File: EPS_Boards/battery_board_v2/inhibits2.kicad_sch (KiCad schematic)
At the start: 6 parts

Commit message: eps: battery board: added AND gate for power control and cleaned up global labels
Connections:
- net EN-D1 is gone; now on net PCM_IN: U?. (VCC)
- net PCM is gone; now on net PCM_IN: C?.2, C?.2, R?.2, U?. (VCC)
- net PCM_IN: now reaches U?. (VCC)
- net VIN renamed HIGH_INHIB_IN
- new net EN_D1: U?. (VCC)
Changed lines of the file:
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@@
     (stroke (width 0) (type default) (color 0 0 0 0))
   )
-  (polyline (pts (xy 245.11 34.29) (xy 245.11 111.76))
+  (polyline (pts (xy 248.92 34.29) (xy 248.92 111.76))
     (stroke (width 0) (type default) (color 0 0 0 0))
   )
@@
     (stroke (width 0) (type default) (color 0 0 0 0))
   )
-  (polyline (pts (xy 144.78 34.29) (xy 245.11 34.29))
+  (polyline (pts (xy 135.89 34.925) (xy 248.92 34.29))
     (stroke (width 0) (type default) (color 0 0 0 0))
   )
@@
     (stroke (width 0) (type default) (color 0 0 0 0))
   )
-  (polyline (pts (xy 245.11 111.76) (xy 144.78 111.76))
+  (polyline (pts (xy 248.92 111.76) (xy 135.89 112.395))
     (stroke (width 0) (type default) (color 0 0 0 0))
   )
@@
     (stroke (width 0) (type default) (color 0 0 0 0))
   )
-  (polyline (pts (xy 144.78 111.76) (xy 144.78 34.29))
+  (polyline (pts (xy 135.89 112.395) (xy 135.89 34.925))
     (stroke (width 0) (type default) (color 0 0 0 0))
   )
@@
     (effects (font (size 1.27 1.27)) (justify left bottom))
   )
-  (global_label "VIN" (shape input) (at 153.67 44.45 180) (fields_autoplaced)
+  (global_label "HIGH_INHIB_IN" (shape input) (at 153.67 44.45 180) (fields_autoplaced)
     (effects (font (size 1.27 1.27)) (justify right))
-    (property "Intersheet References" "${INTERSHEET_REFS}" (id 0) (at 148.322 44.3706 0)
+    (property "Intersheet References" "${INTERSHEET_REFS}" (id 0) (at 137.7991 44.3706 0)
       (effects (font (size 1.27 1.27)) (justify right) hide)
     )
@@
     )
   )
-  (global_label "EN-D1" (shape input) (at 180.34 81.28 180) (fields_autoplaced)
+  (global_label "EN_D1" (shape input) (at 180.34 81.28 180) (fields_autoplaced)
     (effects (font (size 1.27 1.27)) (justify right))
-    (property "Intersheet References" "${INTERSHEET_REFS}" (id 0) (at 171.4844 81.2006 0)
+    (property "Intersheet References" "${INTERSHEET_REFS}" (id 0) (at 172.0891 81.2006 0)
       (effects (font (size 1.27 1.27)) (justify right) hide)
     )
@@
     )
   )
-  (global_label "PCM" (shape input) (at 237.49 44.45 0) (fields_autoplaced)
+  (global_label "PCM_IN" (shape input) (at 237.49 44.45 0) (fields_autoplaced)
     (effects (font (size 1.27 1.27)) (justify left))
-    (property "Intersheet References" "${INTERSHEET_REFS}" (id 0) (at 243.8056 44.3706 0)
+    (property "Intersheet References" "${INTERSHEET_REFS}" (id 0) (at 246.7085 44.3706 0)
       (effects (font (size 1.27 1.27)) (justify left) hide)
     )

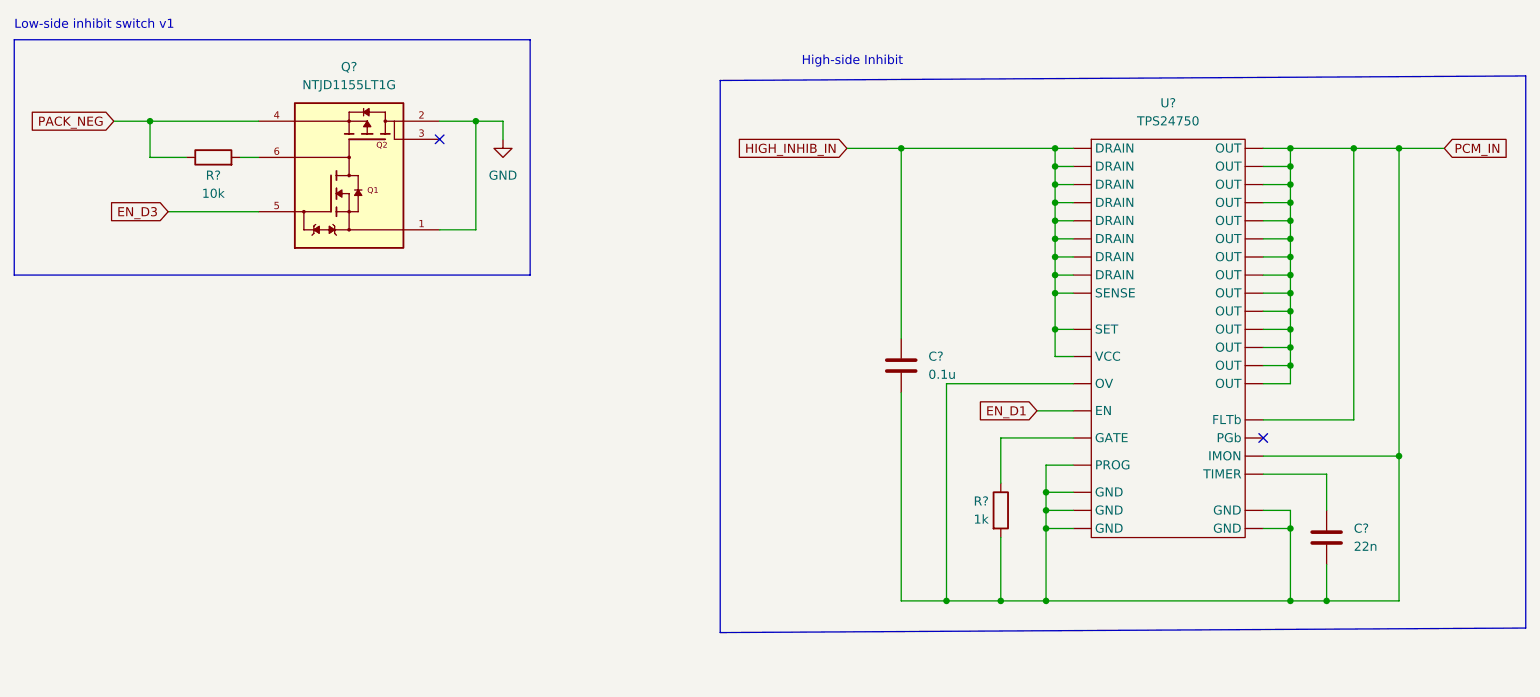
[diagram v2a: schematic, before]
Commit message: eps: battery board: finializing schematic
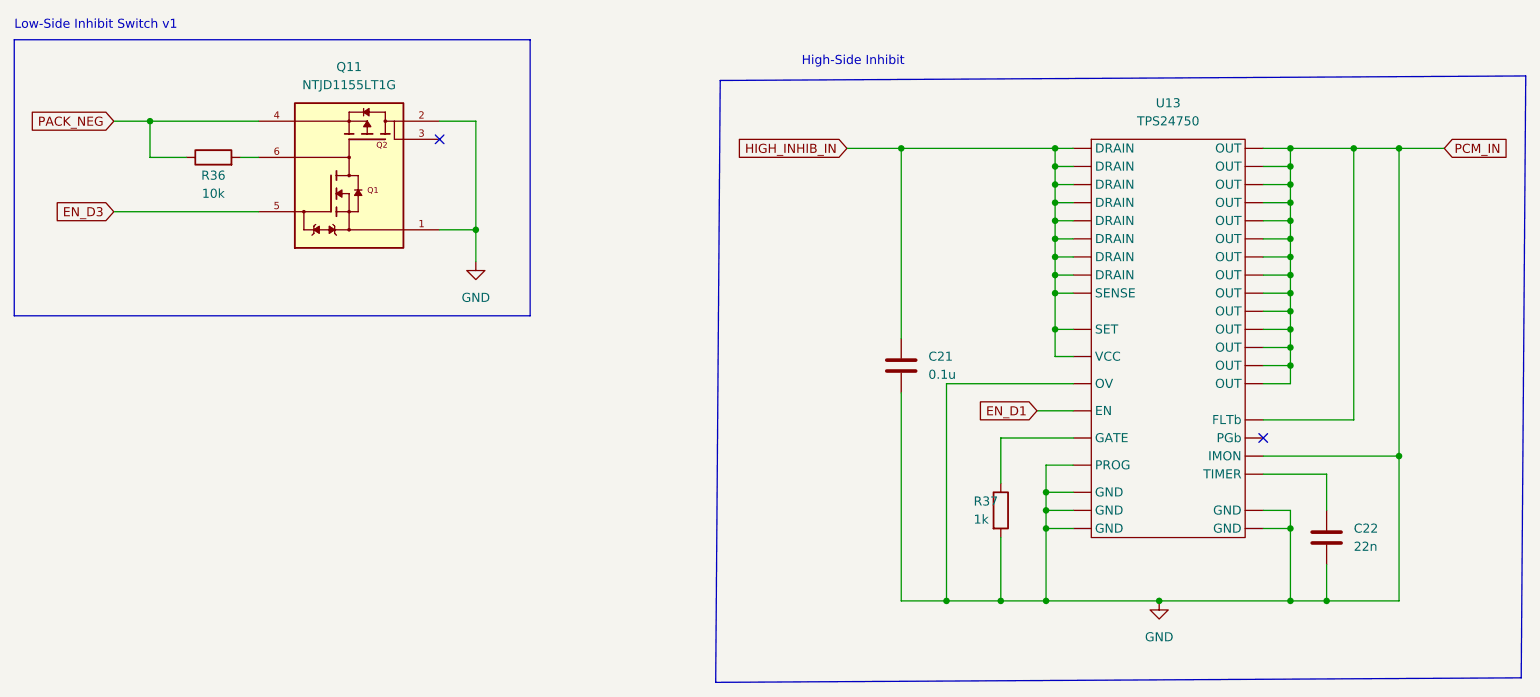
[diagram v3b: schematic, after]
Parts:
- gave numbers to parts that had none: 6
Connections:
- net GND: now also C21.2, C22.2, R37.2, U13. (VCC)
- removed net PCM_IN: C21.2, C22.2, R37.2, U13. (VCC)
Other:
- note added: "High-Side Inhibit"
- note added: "Low-Side Inhibit Switch v1"
- note removed: "High-side Inhibit"
- note removed: "Low-side inhibit switch v1"
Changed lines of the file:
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@@
   (junction (at 215.9 72.39) (diameter 0) (color 0 0 0 0)
   )
+  (junction (at 197.485 107.95) (diameter 0) (color 0 0 0 0)
+  )
   (junction (at 182.88 46.99) (diameter 0) (color 0 0 0 0)
   )
@@
   (junction (at 181.61 97.79) (diameter 0) (color 0 0 0 0)
   )
-  (junction (at 101.6 40.64) (diameter 0) (color 0 0 0 0)
+  (junction (at 101.6 55.88) (diameter 0) (color 0 0 0 0)
   )
   (junction (at 167.64 107.95) (diameter 0) (color 0 0 0 0)
@@
     (stroke (width 0) (type default) (color 0 0 0 0))
   )
+  (wire (pts (xy 197.485 107.95) (xy 215.9 107.95))
+    (stroke (width 0) (type default) (color 0 0 0 0))
+  )
   (wire (pts (xy 215.9 72.39) (xy 215.9 74.93))
     (stroke (width 0) (type default) (color 0 0 0 0))
@@
     (stroke (width 0) (type default) (color 0 0 0 0))
   )
-  (wire (pts (xy 181.61 107.95) (xy 215.9 107.95))
+  (wire (pts (xy 181.61 107.95) (xy 197.485 107.95))
     (stroke (width 0) (type default) (color 0 0 0 0))
   )
@@
     (stroke (width 0) (type default) (color 0 0 0 0))
   )
-  (polyline (pts (xy 248.92 34.29) (xy 248.92 111.76))
-    (stroke (width 0) (type default) (color 0 0 0 0))
-  )
-  (polyline (pts (xy 109.22 62.23) (xy 109.22 29.21))
+  (polyline (pts (xy 248.92 34.29) (xy 248.285 118.745))
+    (stroke (width 0) (type default) (color 0 0 0 0))
+  )
+  (polyline (pts (xy 109.22 67.945) (xy 109.22 29.21))
     (stroke (width 0) (type default) (color 0 0 0 0))
   )
@@
     (stroke (width 0) (type default) (color 0 0 0 0))
   )
-  (wire (pts (xy 58.42 53.34) (xy 71.12 53.34))
+  (wire (pts (xy 50.8 53.34) (xy 71.12 53.34))
     (stroke (width 0) (type default) (color 0 0 0 0))
   )
@@
     (stroke (width 0) (type default) (color 0 0 0 0))
   )
+  (wire (pts (xy 101.6 60.325) (xy 101.6 55.88))
+    (stroke (width 0) (type default) (color 0 0 0 0))
+  )
   (wire (pts (xy 182.88 49.53) (xy 182.88 52.07))
     (stroke (width 0) (type default) (color 0 0 0 0))
@@
     (stroke (width 0) (type default) (color 0 0 0 0))
   )
-  (wire (pts (xy 101.6 40.64) (xy 105.41 40.64))
-    (stroke (width 0) (type default) (color 0 0 0 0))
-  )
   (wire (pts (xy 175.26 99.06) (xy 175.26 107.95))
     (stroke (width 0) (type default) (color 0 0 0 0))
@@
     (stroke (width 0) (type default) (color 0 0 0 0))
   )
-  (polyline (pts (xy 248.92 111.76) (xy 135.89 112.395))
+  (polyline (pts (xy 248.285 118.745) (xy 135.255 119.38))
     (stroke (width 0) (type default) (color 0 0 0 0))
   )
@@
     (stroke (width 0) (type default) (color 0 0 0 0))
   )
-  (polyline (pts (xy 36.83 29.21) (xy 36.83 62.23))
+  (polyline (pts (xy 36.83 29.21) (xy 36.83 67.945))
     (stroke (width 0) (type default) (color 0 0 0 0))
   )
@@
     (stroke (width 0) (type default) (color 0 0 0 0))
   )
-  (polyline (pts (xy 36.83 62.23) (xy 109.22 62.23))
+  (polyline (pts (xy 36.83 67.945) (xy 109.22 67.945))
     (stroke (width 0) (type default) (color 0 0 0 0))
   )
@@
     (stroke (width 0) (type default) (color 0 0 0 0))
   )
-  (wire (pts (xy 105.41 40.64) (xy 105.41 43.18))
-    (stroke (width 0) (type default) (color 0 0 0 0))
-  )
   (wire (pts (xy 212.09 90.17) (xy 220.98 90.17))
     (stroke (width 0) (type default) (color 0 0 0 0))
@@
     (stroke (width 0) (type default) (color 0 0 0 0))
   )
-  (polyline (pts (xy 135.89 112.395) (xy 135.89 34.925))
+  (polyline (pts (xy 135.255 119.38) (xy 135.89 34.925))
     (stroke (width 0) (type default) (color 0 0 0 0))
   )
@@
     (stroke (width 0) (type default) (color 0 0 0 0))
   )
-  (text "Low-side inhibit switch v1\n" (at 36.83 27.94 0)
+  (text "Low-Side Inhibit Switch v1\n" (at 36.83 27.94 0)
     (effects (font (size 1.27 1.27)) (justify left bottom))
   )
-  (text "High-side Inhibit\n" (at 147.32 33.02 0)
+  (text "High-Side Inhibit\n" (at 147.32 33.02 0)
     (effects (font (size 1.27 1.27)) (justify left bottom))
   )
@@
     )
   )
-  (global_label "EN_D3" (shape input) (at 58.42 53.34 180) (fields_autoplaced)
+  (global_label "EN_D3" (shape input) (at 50.8 53.34 180) (fields_autoplaced)
     (effects (font (size 1.27 1.27)) (justify right))
-    (property "Intersheet References" "${INTERSHEET_REFS}" (id 0) (at 50.1691 53.2606 0)
+    (property "Intersheet References" "${INTERSHEET_REFS}" (id 0) (at 42.5491 53.2606 0)
       (effects (font (size 1.27 1.27)) (justify right) hide)
     )
@@
   (symbol (lib_id "Device:R") (at 64.77 45.72 90) (unit 1)
     (in_bom yes) (on_board yes)
-    (property "Reference" "R?" (id 0) (at 64.77 48.26 90))
+    (property "Reference" "R36" (id 0) (at 64.77 48.26 90))
     (property "Value" "10k" (id 1) (at 64.77 50.8 90))
     (property "Footprint" "" (id 2) (at 64.77 47.498 90)
@@
     (pin "2")
   )
-  (symbol (lib_id "power:GND") (at 105.41 43.18 0) (unit 1)
-    (in_bom yes) (on_board yes) (fields_autoplaced)
-    (property "Reference" "#PWR?" (id 0) (at 105.41 49.53 0)
-      (effects (font (size 1.27 1.27)) hide)
-    )
-    (property "Value" "GND" (id 1) (at 105.41 48.26 0))
-    (property "Footprint" "" (id 2) (at 105.41 43.18 0)
-      (effects (font (size 1.27 1.27)) hide)
-    )
-    (property "Datasheet" "" (id 3) (at 105.41 43.18 0)
-      (effects (font (size 1.27 1.27)) hide)
-    )
-    (pin "1")
-  )
   (symbol (lib_id "griffin_Library:TPS24750") (at 199.39 55.88 0) (unit 1)
     (in_bom yes) (on_board yes) (fields_autoplaced)
-    (property "Reference" "U?" (id 0) (at 198.755 38.1 0))
+    (property "Reference" "U13" (id 0) (at 198.755 38.1 0))
     (property "Value" "TPS24750" (id 1) (at 198.755 40.64 0))
     (property "Footprint" "" (id 2) (at 194.31 55.88 0)
@@
     (pin "")
   )
+  (symbol (lib_id "power:GND") (at 197.485 107.95 0) (unit 1)
+    (in_bom yes) (on_board yes) (fields_autoplaced)
+    (property "Reference" "#PWR0119" (id 0) (at 197.485 114.3 0)
+      (effects (font (size 1.27 1.27)) hide)
+    )
+    (property "Value" "GND" (id 1) (at 197.485 113.03 0))
+    (property "Footprint" "" (id 2) (at 197.485 107.95 0)
+      (effects (font (size 1.27 1.27)) hide)
+    )
+    (property "Datasheet" "" (id 3) (at 197.485 107.95 0)
+      (effects (font (size 1.27 1.27)) hide)
+    )
+    (pin "1")
+  )
   (symbol (lib_id "Device:R") (at 175.26 95.25 0) (unit 1)
     (in_bom yes) (on_board yes)
-    (property "Reference" "R?" (id 0) (at 171.45 93.98 0)
+    (property "Reference" "R37" (id 0) (at 171.45 93.98 0)
       (effects (font (size 1.27 1.27)) (justify left))
     )
@@
     (pin "2")
   )
+  (symbol (lib_id "power:GND") (at 101.6 60.325 0) (unit 1)
+    (in_bom yes) (on_board yes) (fields_autoplaced)
+    (property "Reference" "#PWR0118" (id 0) (at 101.6 66.675 0)
+      (effects (font (size 1.27 1.27)) hide)
+    )
+    (property "Value" "GND" (id 1) (at 101.6 65.405 0))
+    (property "Footprint" "" (id 2) (at 101.6 60.325 0)
+      (effects (font (size 1.27 1.27)) hide)
+    )
+    (property "Datasheet" "" (id 3) (at 101.6 60.325 0)
+      (effects (font (size 1.27 1.27)) hide)
+    )
+    (pin "1")
+  )
   (symbol (lib_id "Device:C") (at 220.98 99.06 0) (unit 1)
     (in_bom yes) (on_board yes) (fields_autoplaced)
-    (property "Reference" "C?" (id 0) (at 224.79 97.7899 0)
+    (property "Reference" "C22" (id 0) (at 224.79 97.7899 0)
       (effects (font (size 1.27 1.27)) (justify left))
     )
@@
   (symbol (lib_id "Device:C") (at 161.29 74.93 0) (unit 1)
     (in_bom yes) (on_board yes) (fields_autoplaced)
-    (property "Reference" "C?" (id 0) (at 165.1 73.6599 0)
+    (property "Reference" "C21" (id 0) (at 165.1 73.6599 0)
       (effects (font (size 1.27 1.27)) (justify left))
     )
@@
   (symbol (lib_id "NTJD1155LT1G:NTJD1155LT1G") (at 83.82 48.26 0) (unit 1)
     (in_bom yes) (on_board yes) (fields_autoplaced)
-    (property "Reference" "Q?" (id 0) (at 83.82 33.02 0))
+    (property "Reference" "Q11" (id 0) (at 83.82 33.02 0))
     (property "Value" "NTJD1155LT1G" (id 1) (at 83.82 35.56 0))
     (property "Footprint" "TRANS_NTJD1155LT1G" (id 2) (at 83.82 48.26 0)

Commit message: eps: battery board: updated board layout
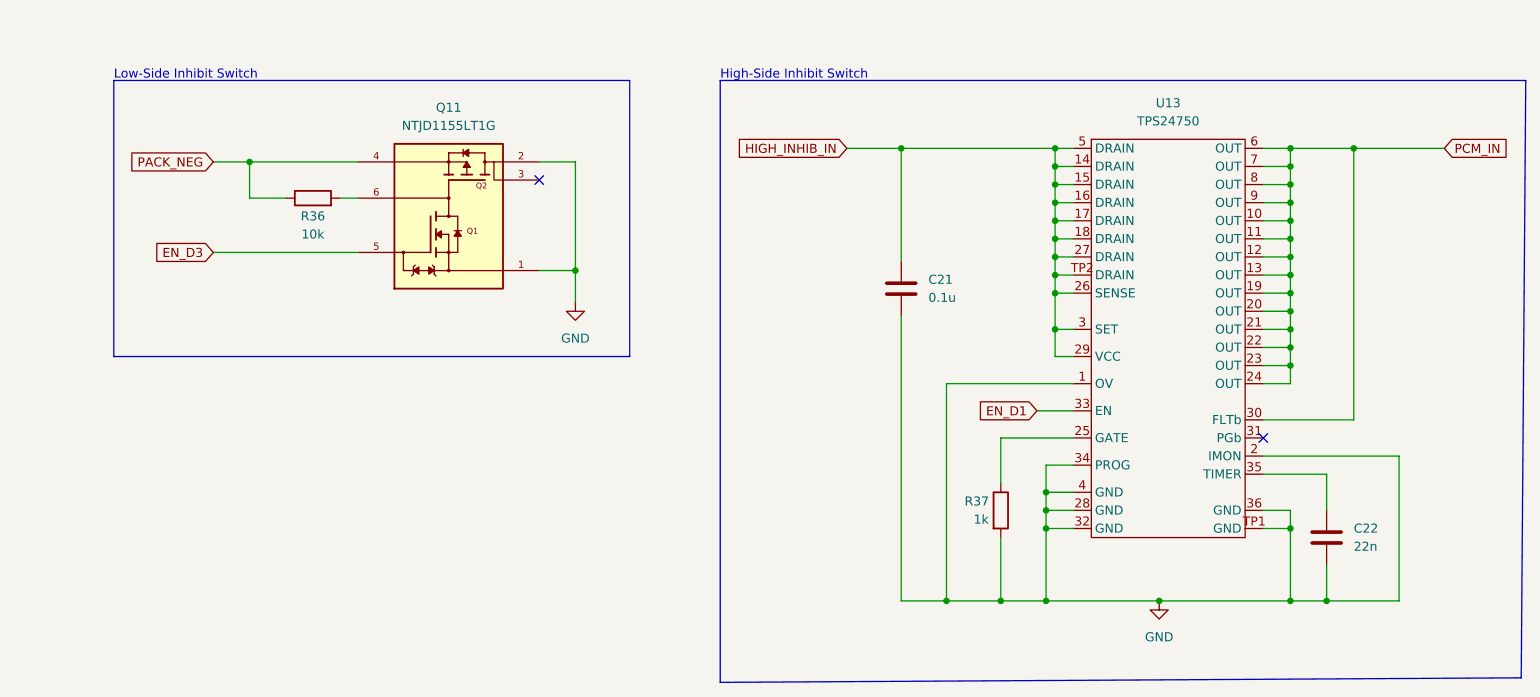
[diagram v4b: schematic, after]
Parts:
- removed U13: TPS24750, symbol griffin_Library:TPS24750
- added U13: TPS24750, qset-footprints:TPS24750, symbol TPS24750:TPS24750
- C21, C22: footprint (none) -> Capacitor_SMD:C_01005_0402Metric
- R36, R37: footprint (none) -> Resistor_SMD:R_0402_1005Metric
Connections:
- net EN_D1: now also U13.33 (EN)
- net GND: now also U13.1 (OV), U13.2 (IMON), U13.28 (GND), U13.32 (GND), U13.34 (PROG), U13.36 (GND), U13.4 (GND), U13.TP1 (GND)
- net HIGH_INHIB_IN: now also U13.14 (DRAIN), U13.15 (DRAIN), U13.16 (DRAIN), U13.17 (DRAIN), U13.18 (DRAIN), U13.26 (SENSE), U13.27 (DRAIN), U13.29 (VCC), U13.3 (SET), U13.5 (DRAIN), U13.TP2 (DRAIN)
- net at R37.1: now also U13.25 (GATE)
- net at C22.1: now also U13.35 (TIMER)
- new net PCM_IN: U13.10 (OUT), U13.11 (OUT), U13.12 (OUT), U13.13 (OUT), U13.19 (OUT), U13.20 (OUT), U13.21 (OUT), U13.22 (OUT), U13.23 (OUT), U13.24 (OUT), U13.30 (FLTb), U13.6 (OUT), U13.7 (OUT), U13.8 (OUT), U13.9 (OUT)
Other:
- note added: "High-Side Inhibit Switch"
- note added: "Low-Side Inhibit Switch"
- note removed: "High-Side Inhibit"
- note removed: "Low-Side Inhibit Switch v1"
- moved on the sheet: C21, Q11, R36

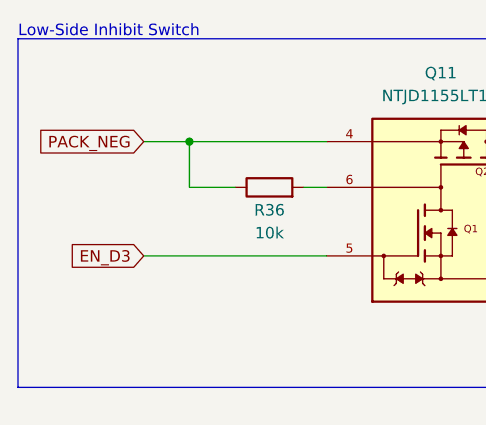
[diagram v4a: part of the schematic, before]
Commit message: eps: battery board: more updates to layout
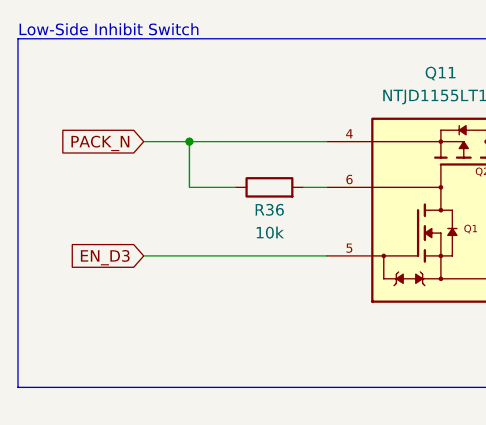
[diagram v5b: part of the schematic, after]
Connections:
- net PACK_NEG renamed PACK_N
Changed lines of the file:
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@@
     )
   )
-  (global_label "PACK_NEG" (shape input) (at 64.77 46.355 180) (fields_autoplaced)
+  (global_label "PACK_N" (shape input) (at 64.77 46.355 180) (fields_autoplaced)
     (effects (font (size 1.27 1.27)) (justify right))
-    (property "Intersheet References" "${INTERSHEET_REFS}" (id 0) (at 52.8301 46.2756 0)
+    (property "Intersheet References" "${INTERSHEET_REFS}" (id 0) (at 55.2491 46.2756 0)
       (effects (font (size 1.27 1.27)) (justify right) hide)
     )

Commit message: eps: battery board: progress on pcb layout
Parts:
- Q11: footprint TRANS_NTJD1155LT1G -> qset-footprints:TRANS_NTJD1155LT1G
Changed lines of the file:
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@@
   )
   (symbol (lib_id "Device:C") (at 161.29 64.135 0) (unit 1)
-    (in_bom yes) (on_board yes) (fields_autoplaced)
+    (in_bom yes) (on_board yes)
     (property "Reference" "C21" (id 0) (at 165.1 62.8649 0)
       (effects (font (size 1.27 1.27)) (justify left))
@@
     (property "Reference" "Q11" (id 0) (at 97.79 38.735 0))
     (property "Value" "NTJD1155LT1G" (id 1) (at 97.79 41.275 0))
-    (property "Footprint" "TRANS_NTJD1155LT1G" (id 2) (at 97.79 53.975 0)
+    (property "Footprint" "qset-footprints:TRANS_NTJD1155LT1G" (id 2) (at 97.79 53.975 0)
       (effects (font (size 1.27 1.27)) (justify bottom) hide)
     )
-    (property "Datasheet" "" (id 3) (at 97.79 53.975 0)
+    (property "Datasheet" "https://www.onsemi.com/pdf/datasheet/ntjd1155l-d.pdf" (id 3) (at 97.79 53.975 0)
       (effects (font (size 1.27 1.27)) hide)
     )
